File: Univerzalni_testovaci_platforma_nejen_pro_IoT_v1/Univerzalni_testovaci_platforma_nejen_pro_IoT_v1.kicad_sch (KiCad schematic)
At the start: 122 parts, among them J1 Conn_01x10_Male, J10 Conn_01x10_Male, J11 Conn_01x10_Male, J12 Conn_01x10_Male, J2 Conn_01x10_Male, J3 Conn_01x10_Male, J4 Conn_01x10_Male, J5 Conn_02x03_Counter_Clockwise, J6 USB_C_Receptacle, J7 Conn_01x10_Male, J8 Conn_01x10_Male, J9 Conn_01x10_Male, SW1 SW_MEC_5E, U1 STM32F103ZETx, U2 AMS1117-3.3, U3 ESP32-DEVKITC-32D, U4 ESP32-S3, Y1 12Mhz

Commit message: jdu to objednat
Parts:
- added J13: Conn_01x10_Male, Connector_PinHeader_2.54mm:PinHeader_1x10_P2.54mm_Vertical, symbol Connector:Conn_01x10_Male
- D1: value BLUE -> RED; LCSC C72041 -> C2286
- H1, H2, H3, H4, J1, J10, J11, J12, J2, J3, J4, J7, J8, J9, U3: JLCPCB_IGNORE (none) -> 1
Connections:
- net +3V3: now also J13.1 (Pin_1), J13.10 (Pin_10), J13.2 (Pin_2), J13.3 (Pin_3), J13.4 (Pin_4), J13.5 (Pin_5), J13.6 (Pin_6), J13.7 (Pin_7), J13.8 (Pin_8), J13.9 (Pin_9)

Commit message: změna usměrňovače napětí na správný
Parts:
- U2: LCSC C841797 -> C73181
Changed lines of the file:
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@@
       (effects (font (size 1.27 1.27)) hide)
     )
-    (property "LCSC" "C841797" (id 4) (at 327.66 29.21 0)
+    (property "LCSC" "C73181" (id 4) (at 327.66 29.21 0)
       (effects (font (size 1.27 1.27)) hide)
     )

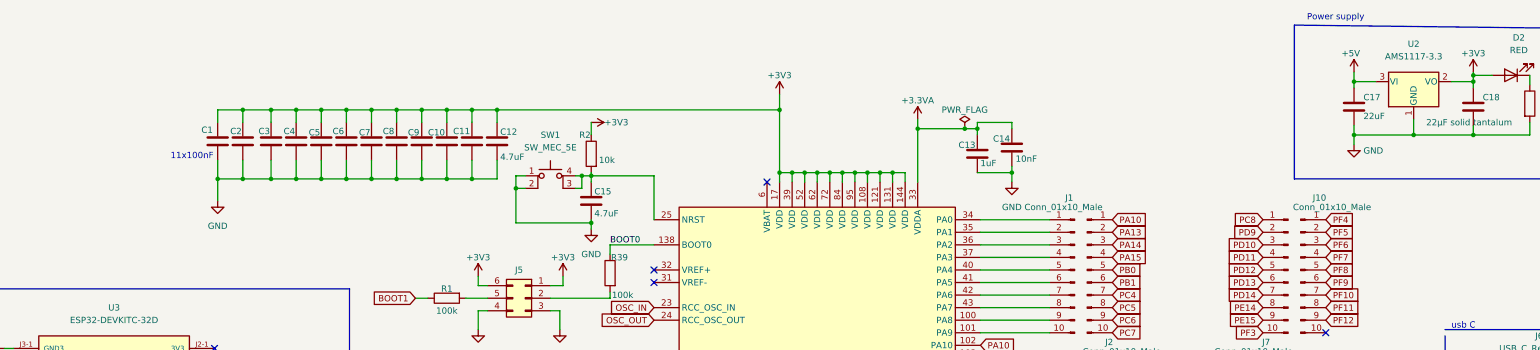
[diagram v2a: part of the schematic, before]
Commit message: změny schématu pro lepší focení
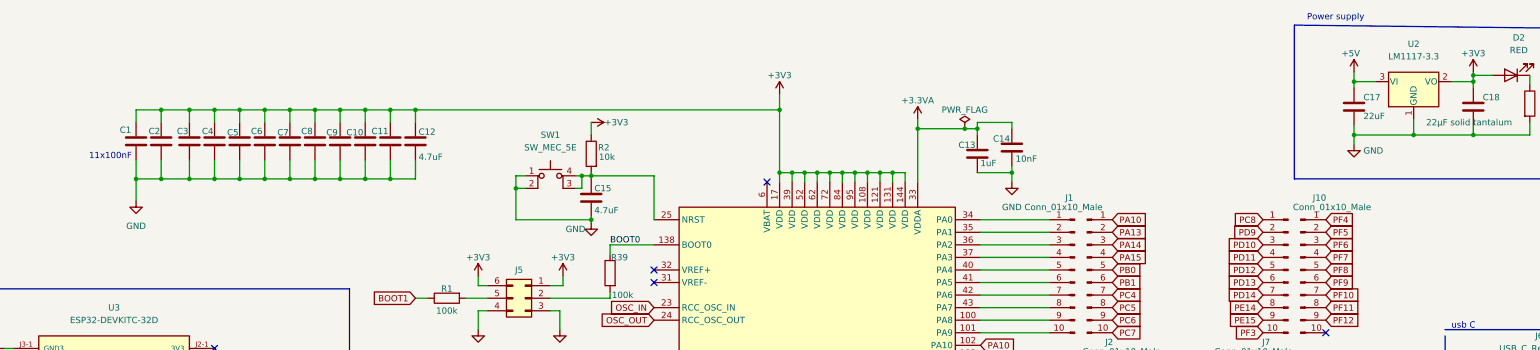
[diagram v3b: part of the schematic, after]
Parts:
- U2: value AMS1117-3.3 -> LM1117-3.3
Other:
- moved on the sheet: C1, C10, C11, C12, C15, C2, C3, C4, C5, C6, C7, C8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
